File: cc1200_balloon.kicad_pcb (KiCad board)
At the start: 4 copper layers, 50 x 30 mm, 105 parts, among them J101 BATT pads, J201 LoRa ANT pads, J202 SWD+DBG pads, J301 434MHz ANT pads, J401 GNSS ANT, J501 BMV080, Q101 DMG3401LSN-7, U201 Wio-E5, U301 CC1200, U401 AT6558R-5N32, U501 SCD40-D-R2, U502 AS3935-BQFT, U503 BME688, U504 BME688, X301 40MHz, X401 TCXO 26MHz, X402 32.768kHz

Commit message: More routing, adjusting traces. Layout silkscreen.
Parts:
- moved TP401 25.7 mm to (91.5, 94.2), turned to -90 degrees
- moved TP302 24.8 mm to (98.3, 100.3)
- moved TP402 23.4 mm to (91.5, 92.2), turned to -90 degrees
- moved TP301 22.3 mm to (93.7, 97.3)
- moved X401 1.14 mm to (84.4, 99.2)
- moved C318 0.72 mm to (104.2, 101.7)
- moved C319 0.40 mm to (102.3, 101.3)
- moved R403 0.20 mm to (91.2, 92.0)
- moved R402 0.20 mm to (91.2, 90.9)
- moved C302 0.20 mm to (100.6, 99.4)
- moved C410 0.19 mm to (82.5, 93.2)
- moved C411 0.13 mm to (82.5, 94.3)
- moved C508 0.05 mm to (111.8, 105.8)
- turned X301 to 90 degrees
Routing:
- net /CC1200 Radio/RADIO_GPIO0: track 0.00 -> 7.01 mm, vias 0 -> 1
- net /CC1200 Radio/RADIO_GPIO3: track 0.00 -> 3.09 mm, vias 0 -> 1
- net +BATT: track 59.1 -> 61.9 mm, vias 41 -> 42
- net /GNSS/GNSS_TMS: track 0.00 -> 2.58 mm, vias 0 -> 1
- net /GNSS/GNSS_TCK: track 0.00 -> 2.55 mm, vias 0 -> 1
- net /CC1200 Radio/XOSC_Q2: track 3.71 -> 6.24 mm
- net /CC1200 Radio/XOSC_Q1: track 7.75 -> 6.09 mm
- net /GNSS/GNSS_VX: track 6.92 -> 5.42 mm
- net /GNSS/GNSS_XREF: track 4.58 -> 3.09 mm
- net SPI_SCK: track 23.0 -> 24.0 mm
- net /MCU/SWDIO: track 9.84 -> 10.7 mm
- net /MCU/BATT_VSENSE: track 9.47 -> 10.0 mm
- net GND: vias 108 -> 198
- net /MCU/DBG_TX: vias 2 -> 1
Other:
- board text added: "-BATT+"
- board text added: "-GND"
- board text added: "-SEL"
- board text added: "SWD"

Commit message: Small adjustments.
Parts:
- moved H104 48.1 mm to (89.5, 102.4)
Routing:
- net RADIO_IRQ: track 25.8 -> 26.7 mm
- net +BATT: track 61.9 -> 61.4 mm
- net GND: vias 198 -> 231
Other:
- board text added: "BATT"
- board text added: "GND"
- board text added: "NRST"
- board text added: "SWCLK"
- board text added: "SWIO"
- board text added: "TX"

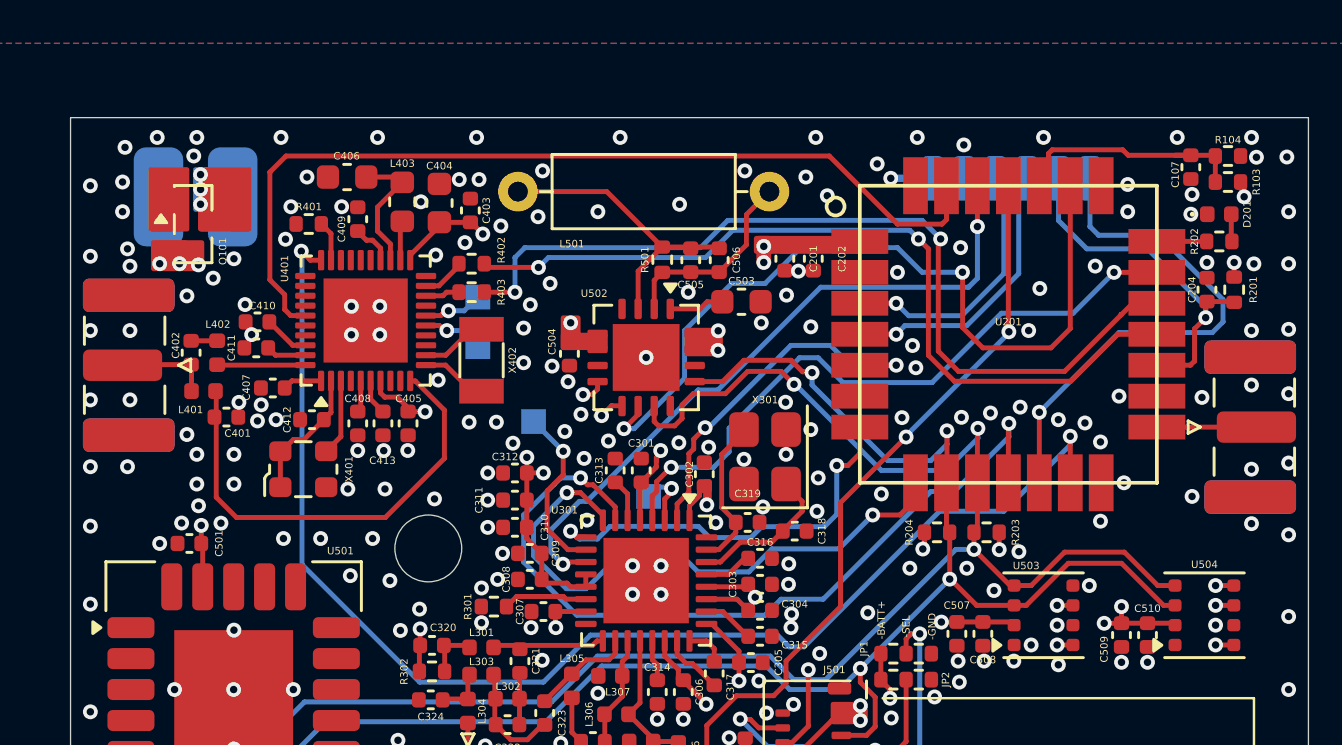
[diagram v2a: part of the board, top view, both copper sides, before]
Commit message: Fix DRC errors.
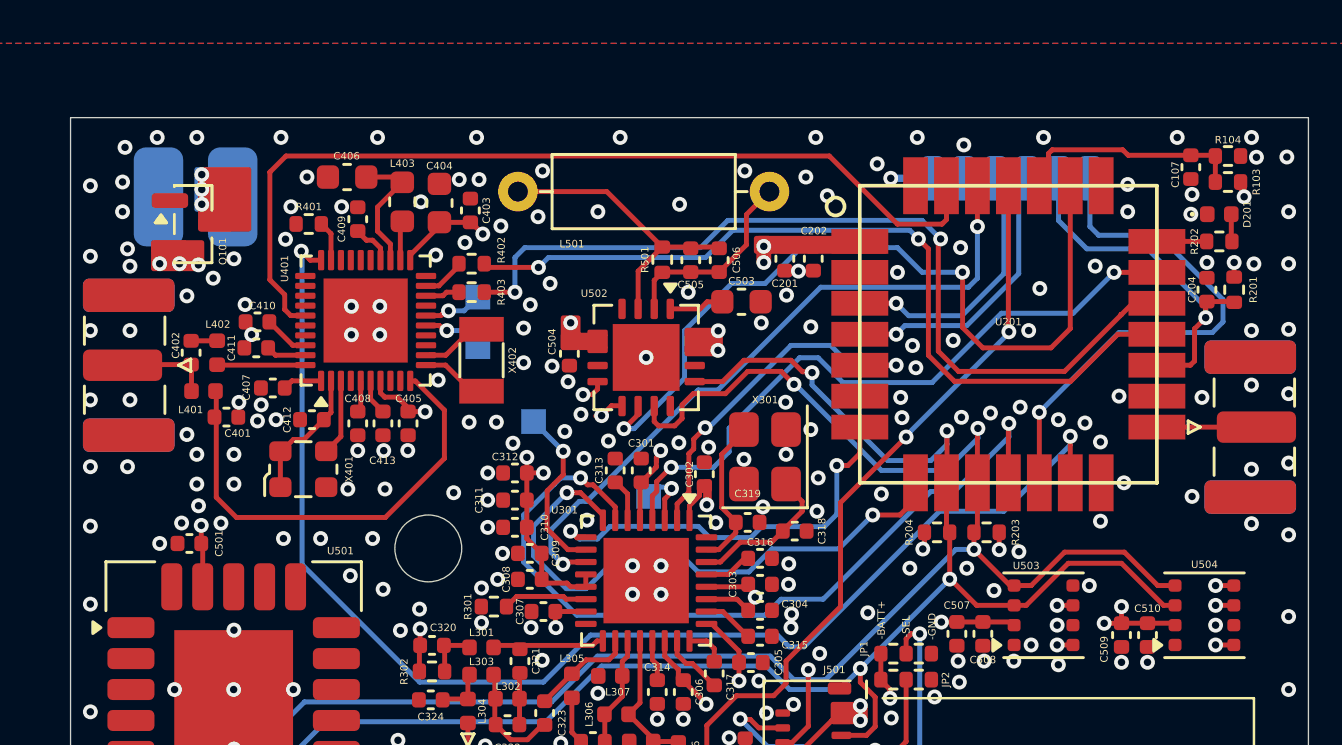
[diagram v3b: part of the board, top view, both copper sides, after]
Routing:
- net /MCU/BATT_VSENSE: track 10.0 -> 9.41 mm
- net GND: vias 231 -> 232
